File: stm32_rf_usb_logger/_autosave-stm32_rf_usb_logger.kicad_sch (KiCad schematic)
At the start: 38 parts, among them J1 SWD, J2 USB_B_Micro, J3 Conn_Coaxial, U1 XC6206PxxxMR, U2 STM32L432KBUx, U3 USBLC6-2SC6, U4 nRF24L01P, Y2 16MHz

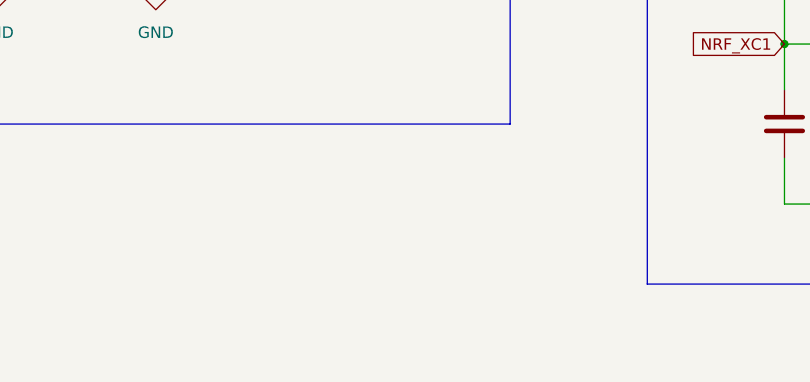
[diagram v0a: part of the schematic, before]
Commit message: completed layout
Layout completed . However, minor changes have to be made regarding fills and pours.
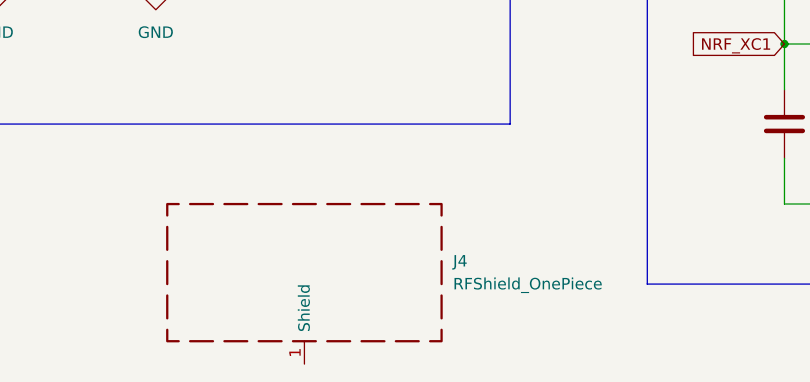
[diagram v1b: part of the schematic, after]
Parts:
- added J4: RFShield_OnePiece, symbol Device:RFShield_OnePiece
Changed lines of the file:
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@@
+    )
+  )
+  (symbol (lib_id "Device:RFShield_OnePiece") (at 69.85 180.34 0) (unit 1)
+    (in_bom yes) (on_board yes) (dnp no) (fields_autoplaced)
+    (property "Reference" "J4" (at 86.36 179.07 0)
+      (effects (font (size 1.27 1.27)) (justify left))
+    )
+    (property "Value" "RFShield_OnePiece" (at 86.36 181.61 0)
+      (effects (font (size 1.27 1.27)) (justify left))
+    )
+    (property "Footprint" "" (at 69.85 182.88 0)
+      (effects (font (size 1.27 1.27)) hide)
+    )
+    (property "Datasheet" "~" (at 69.85 182.88 0)
+      (effects (font (size 1.27 1.27)) hide)
+    )
+    (pin "1")
+    (instances
+      (project "stm32_rf_usb_logger"
+        (path "/dd14fd82-9e8e-4c5a-80f3-7f076ed757ea"
+          (reference "J4") (unit 1)
+        )
+      )
     )
   )
